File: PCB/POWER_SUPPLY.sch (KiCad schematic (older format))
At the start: 14 parts

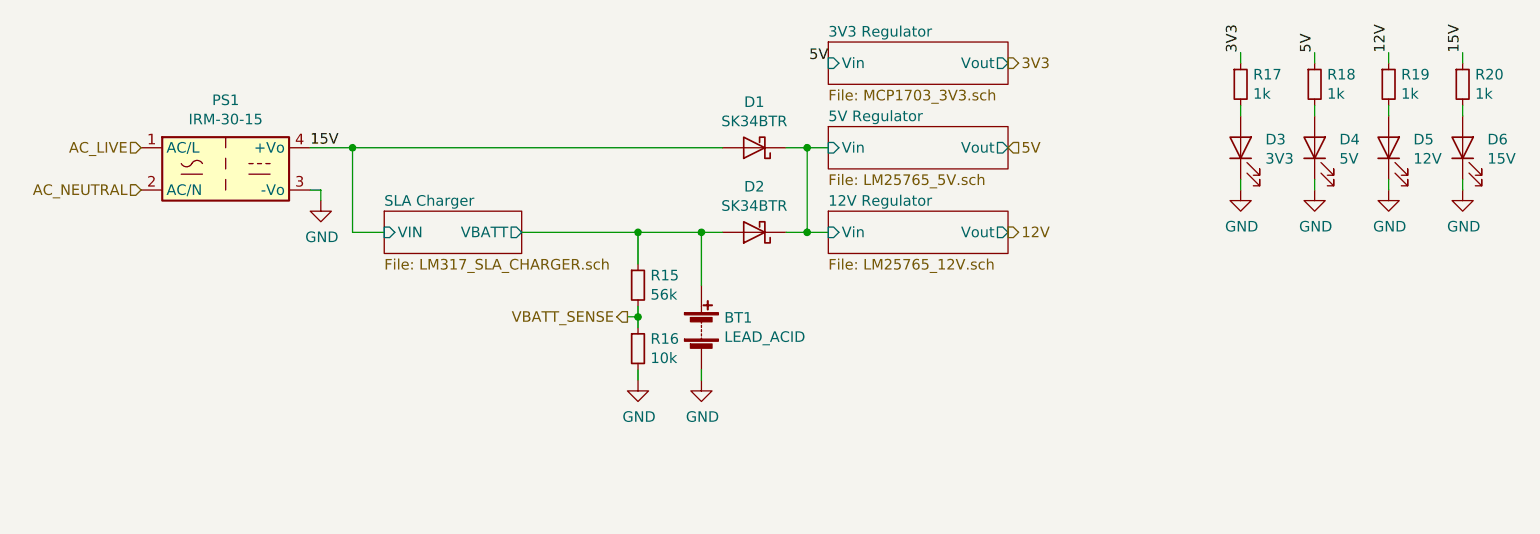
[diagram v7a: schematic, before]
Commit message: Added test points to PSU
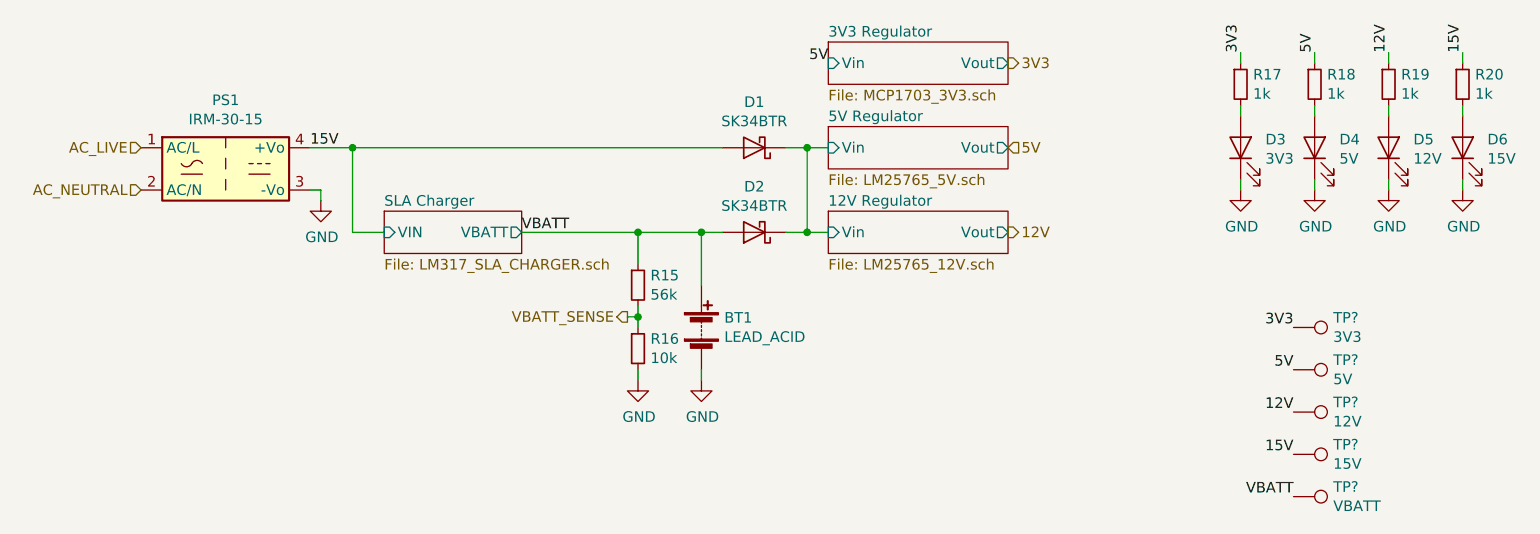
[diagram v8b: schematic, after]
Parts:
- added TP?: 3V3, symbol Connector:TestPoint
- added TP?: 5V, symbol Connector:TestPoint
- added TP?: 12V, symbol Connector:TestPoint
- added TP?: 15V, symbol Connector:TestPoint
- added TP?: VBATT, symbol Connector:TestPoint
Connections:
- net 12V: now also TP?.1
- net 15V: now also TP?.1
- net 3V3: now also TP?.1
- net 5V: now also TP?.1
- net SLA Charger/VBATT renamed VBATT
- net VBATT: now also TP?.1
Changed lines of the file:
@@
 Text Label 6200 2400 2    50   ~ 0
 5V
+$Comp
+L Connector:TestPoint TP?
+U 1 1 5E9A7893
+P 8400 3650
+AR Path="/5E9A7893" Ref="TP?"  Part="1"
+AR Path="/5E880E11/5E9A7893" Ref="TP?"  Part="1"
+F 0 "TP?" V 8354 3838 50  0000 L CNN
+F 1 "3V3" V 8445 3838 50  0000 L CNN
+F 2 "" H 8600 3650 50  0001 C CNN
+F 3 "~" H 8600 3650 50  0001 C CNN
+	1    8400 3650
+	0    1    1    0
+$EndComp
+$Comp
+L Connector:TestPoint TP?
+U 1 1 5E9A813E
+P 8400 3850
+AR Path="/5E9A813E" Ref="TP?"  Part="1"
+AR Path="/5E880E11/5E9A813E" Ref="TP?"  Part="1"
+F 0 "TP?" V 8354 4038 50  0000 L CNN
+F 1 "5V" V 8445 4038 50  0000 L CNN
+F 2 "" H 8600 3850 50  0001 C CNN
+F 3 "~" H 8600 3850 50  0001 C CNN
+	1    8400 3850
+	0    1    1    0
+$EndComp
+$Comp
+L Connector:TestPoint TP?
+U 1 1 5E9A8480
+P 8400 4050
+AR Path="/5E9A8480" Ref="TP?"  Part="1"
+AR Path="/5E880E11/5E9A8480" Ref="TP?"  Part="1"
+F 0 "TP?" V 8354 4238 50  0000 L CNN
+F 1 "12V" V 8445 4238 50  0000 L CNN
+F 2 "" H 8600 4050 50  0001 C CNN
+F 3 "~" H 8600 4050 50  0001 C CNN
+	1    8400 4050
+	0    1    1    0
+$EndComp
+$Comp
+L Connector:TestPoint TP?
+U 1 1 5E9A87D2
+P 8400 4250
+AR Path="/5E9A87D2" Ref="TP?"  Part="1"
+AR Path="/5E880E11/5E9A87D2" Ref="TP?"  Part="1"
+F 0 "TP?" V 8354 4438 50  0000 L CNN
+F 1 "15V" V 8445 4438 50  0000 L CNN
+F 2 "" H 8600 4250 50  0001 C CNN
+F 3 "~" H 8600 4250 50  0001 C CNN
+	1    8400 4250
+	0    1    1    0
+$EndComp
+$Comp
+L Connector:TestPoint TP?
+U 1 1 5E9A9A9D
+P 8400 4450
+AR Path="/5E9A9A9D" Ref="TP?"  Part="1"
+AR Path="/5E880E11/5E9A9A9D" Ref="TP?"  Part="1"
+F 0 "TP?" V 8354 4638 50  0000 L CNN
+F 1 "VBATT" V 8445 4638 50  0000 L CNN
+F 2 "" H 8600 4450 50  0001 C CNN
+F 3 "~" H 8600 4450 50  0001 C CNN
+	1    8400 4450
+	0    1    1    0
+$EndComp
+Text Label 8400 3650 2    50   ~ 0
+3V3
+Text Label 8400 3850 2    50   ~ 0
+5V
+Text Label 8400 4050 2    50   ~ 0
+12V
+Text Label 8400 4250 2    50   ~ 0
+15V
+Text Label 4750 3200 0    50   ~ 0
+VBATT
+Text Label 8400 4450 2    50   ~ 0
+VBATT
 $EndSCHEMATC
